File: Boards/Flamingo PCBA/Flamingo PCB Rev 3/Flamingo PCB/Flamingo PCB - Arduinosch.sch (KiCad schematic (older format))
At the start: 7 parts

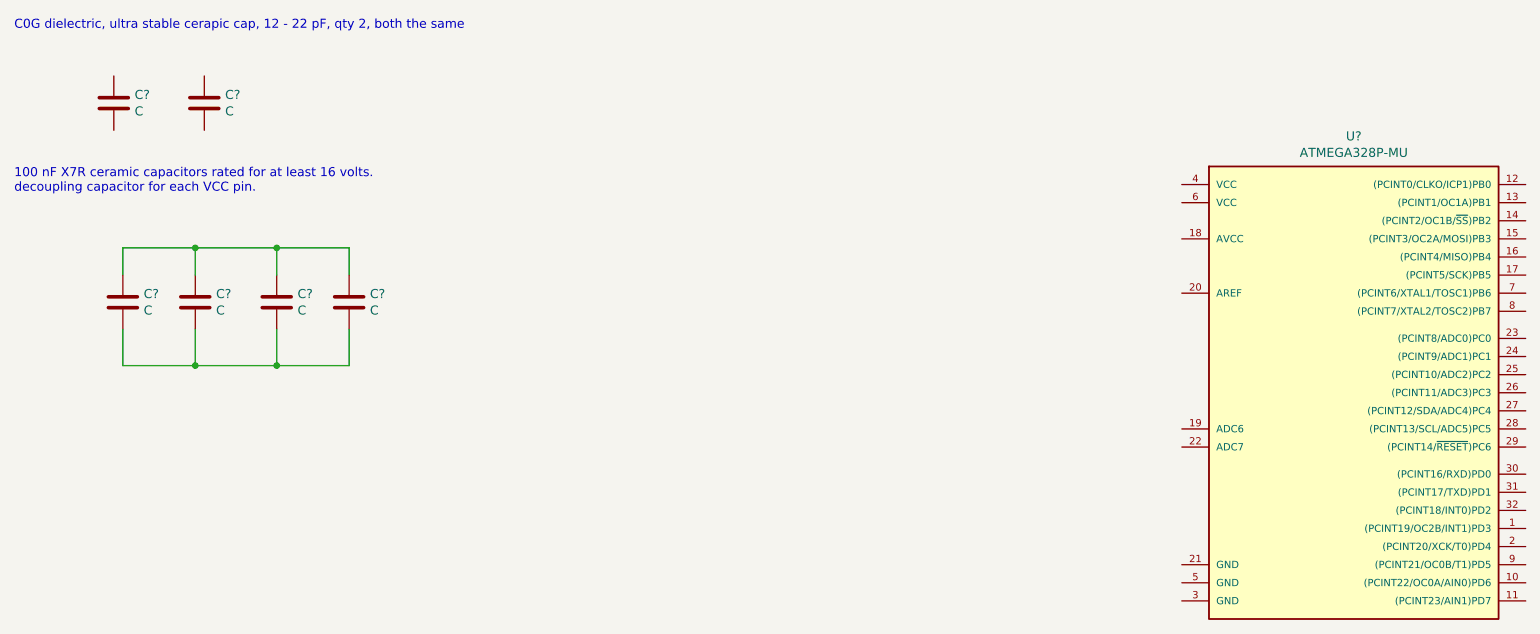
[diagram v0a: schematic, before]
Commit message: Advanced schematic for battery charger
To do:

* Find a better connector for the switch than a JST PH2
* Check the polarity of the battery connector w.r.t. Adafruit batteries.
*Assign footprints
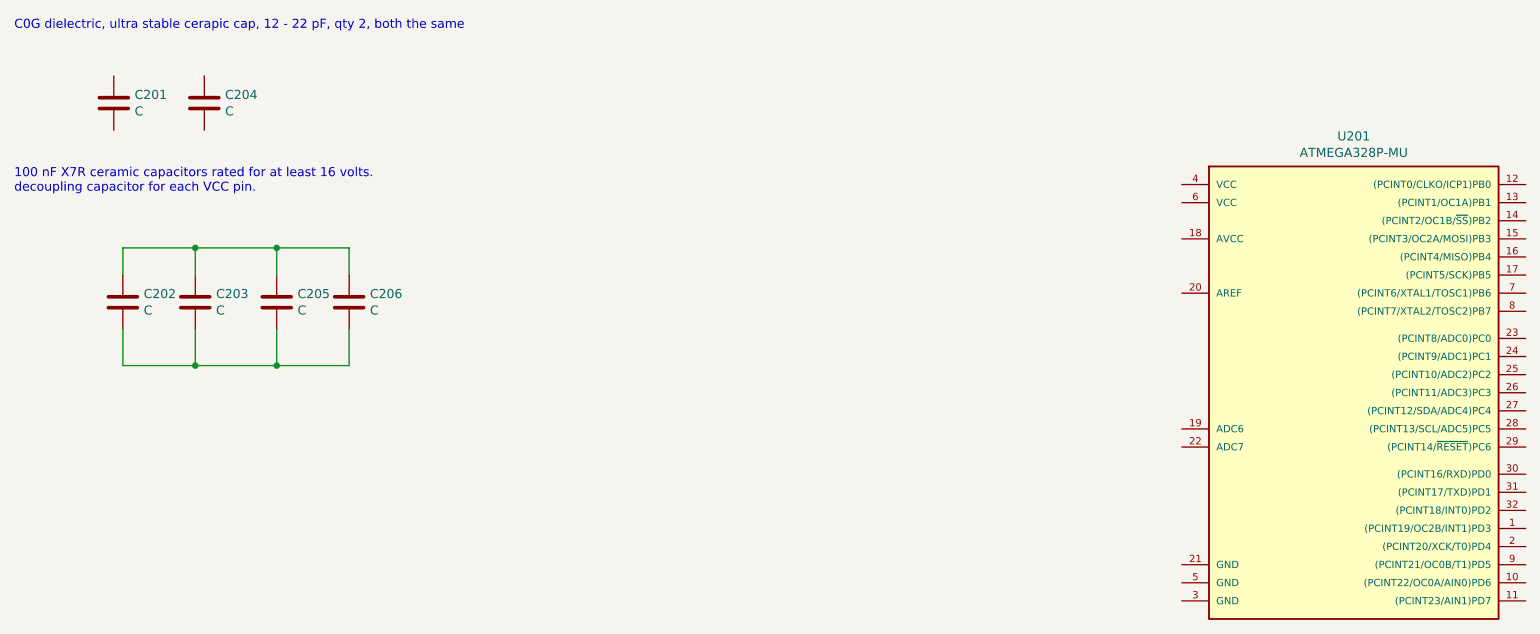
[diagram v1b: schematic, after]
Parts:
- C201, C202, C203, C204, C205, C206: renamed from C?; Description (none) -> -; Digi-Key_PN (none) -> -; MFR P/N (none) -> MFR P/N; Manufacturer (none) -> -; Website (none) -> -
- U201: renamed from U?; Description (none) -> -; Digi-Key_PN (none) -> -; MFR P/N (none) -> MFR P/N; Manufacturer (none) -> -; Website (none) -> -
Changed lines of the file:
@@
 $EndDescr
 $Comp
-L Device:C C?
+L Device:C C201
 U 1 1 5F78D849
 P 1250 1550
-F 0 "C?" H 1365 1596 50  0000 L CNN
+F 0 "C201" H 1365 1596 50  0000 L CNN
 F 1 "C" H 1365 1505 50  0000 L CNN
 F 2 "" H 1288 1400 50  0001 C CNN
 F 3 "~" H 1250 1550 50  0001 C CNN
+F 4 "-" H 1250 1550 50  0001 C CNN "Description"
+F 5 "MFR P/N" H 1250 1550 50  0001 C CNN "MFR P/N"
+F 6 "-" H 1250 1550 50  0001 C CNN "Manufacturer"
+F 7 "-" H 1250 1550 50  0001 C CNN "Website"
+F 8 "-" H 1250 1550 50  0001 C CNN "Digi-Key_PN"
 	1    1250 1550
 	1    0    0    -1
@@
 C0G dielectric, ultra stable cerapic cap, 12 - 22 pF, qty 2, both the same
 $Comp
-L Device:C C?
+L Device:C C204
 U 1 1 5F78FF1B
 P 1750 1550
-F 0 "C?" H 1865 1596 50  0000 L CNN
+F 0 "C204" H 1865 1596 50  0000 L CNN
 F 1 "C" H 1865 1505 50  0000 L CNN
 F 2 "" H 1788 1400 50  0001 C CNN
 F 3 "~" H 1750 1550 50  0001 C CNN
+F 4 "-" H 1750 1550 50  0001 C CNN "Description"
+F 5 "MFR P/N" H 1750 1550 50  0001 C CNN "MFR P/N"
+F 6 "-" H 1750 1550 50  0001 C CNN "Manufacturer"
+F 7 "-" H 1750 1550 50  0001 C CNN "Website"
+F 8 "-" H 1750 1550 50  0001 C CNN "Digi-Key_PN"
 	1    1750 1550
 	1    0    0    -1
@@
 100 nF X7R ceramic capacitors rated for at least 16 volts. \ndecoupling capacitor for each VCC pin.
 $Comp
-L Device:C C?
+L Device:C C202
 U 1 1 5F79041B
 P 1300 2650
-F 0 "C?" H 1415 2696 50  0000 L CNN
+F 0 "C202" H 1415 2696 50  0000 L CNN
 F 1 "C" H 1415 2605 50  0000 L CNN
 F 2 "" H 1338 2500 50  0001 C CNN
 F 3 "~" H 1300 2650 50  0001 C CNN
+F 4 "-" H 1300 2650 50  0001 C CNN "Description"
+F 5 "MFR P/N" H 1300 2650 50  0001 C CNN "MFR P/N"
+F 6 "-" H 1300 2650 50  0001 C CNN "Manufacturer"
+F 7 "-" H 1300 2650 50  0001 C CNN "Website"
+F 8 "-" H 1300 2650 50  0001 C CNN "Digi-Key_PN"
 	1    1300 2650
 	1    0    0    -1
 $EndComp
 $Comp
-L Device:C C?
+L Device:C C203
 U 1 1 5F790A46
 P 1700 2650
-F 0 "C?" H 1815 2696 50  0000 L CNN
+F 0 "C203" H 1815 2696 50  0000 L CNN
 F 1 "C" H 1815 2605 50  0000 L CNN
 F 2 "" H 1738 2500 50  0001 C CNN
 F 3 "~" H 1700 2650 50  0001 C CNN
+F 4 "-" H 1700 2650 50  0001 C CNN "Description"
+F 5 "MFR P/N" H 1700 2650 50  0001 C CNN "MFR P/N"
+F 6 "-" H 1700 2650 50  0001 C CNN "Manufacturer"
+F 7 "-" H 1700 2650 50  0001 C CNN "Website"
+F 8 "-" H 1700 2650 50  0001 C CNN "Digi-Key_PN"
 	1    1700 2650
 	1    0    0    -1
 $EndComp
 $Comp
-L Device:C C?
+L Device:C C205
 U 1 1 5F790FAC
 P 2150 2650
-F 0 "C?" H 2265 2696 50  0000 L CNN
+F 0 "C205" H 2265 2696 50  0000 L CNN
 F 1 "C" H 2265 2605 50  0000 L CNN
 F 2 "" H 2188 2500 50  0001 C CNN
 F 3 "~" H 2150 2650 50  0001 C CNN
+F 4 "-" H 2150 2650 50  0001 C CNN "Description"
+F 5 "MFR P/N" H 2150 2650 50  0001 C CNN "MFR P/N"
+F 6 "-" H 2150 2650 50  0001 C CNN "Manufacturer"
+F 7 "-" H 2150 2650 50  0001 C CNN "Website"
+F 8 "-" H 2150 2650 50  0001 C CNN "Digi-Key_PN"
 	1    2150 2650
 	1    0    0    -1
 $EndComp
 $Comp
-L Device:C C?
+L Device:C C206
 U 1 1 5F79155A
 P 2550 2650
-F 0 "C?" H 2665 2696 50  0000 L CNN
+F 0 "C206" H 2665 2696 50  0000 L CNN
 F 1 "C" H 2665 2605 50  0000 L CNN
 F 2 "" H 2588 2500 50  0001 C CNN
 F 3 "~" H 2550 2650 50  0001 C CNN
+F 4 "-" H 2550 2650 50  0001 C CNN "Description"
+F 5 "MFR P/N" H 2550 2650 50  0001 C CNN "MFR P/N"
+F 6 "-" H 2550 2650 50  0001 C CNN "Manufacturer"
+F 7 "-" H 2550 2650 50  0001 C CNN "Website"
+F 8 "-" H 2550 2650 50  0001 C CNN "Digi-Key_PN"
 	1    2550 2650
 	1    0    0    -1
@@
 	1700 3000 2150 3000
 $Comp
-L MyICs:ATMEGA328P-MU U?
+L MyICs:ATMEGA328P-MU U201
 U 1 1 5F7DA94B
 P 8050 3100
-F 0 "U?" H 8100 4467 50  0000 C CNN
+F 0 "U201" H 8100 4467 50  0000 C CNN
 F 1 "ATMEGA328P-MU" H 8100 4376 50  0000 C CNN
 F 2 "MLF/QFN32" H 8050 3100 50  0001 C CIN
 F 3 "" H 8050 3100 50  0001 C CNN
+F 4 "-" H 8050 3100 50  0001 C CNN "Description"
+F 5 "MFR P/N" H 8050 3100 50  0001 C CNN "MFR P/N"
+F 6 "-" H 8050 3100 50  0001 C CNN "Manufacturer"
+F 7 "-" H 8050 3100 50  0001 C CNN "Website"
+F 8 "-" H 8050 3100 50  0001 C CNN "Digi-Key_PN"
 	1    8050 3100
 	1    0    0    -1
